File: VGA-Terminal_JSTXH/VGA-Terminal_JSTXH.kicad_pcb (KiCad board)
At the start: 2 copper layers, 51 x 44 mm, 12 parts, among them J1 DB15_Female_HighDensity_Mount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, J2 Thermistor, J3 Heater, J4 E3D Fan, J5 X Endstop, J6 Z Endstop, J7 GND & Pin14, J8 Part Fan, J9 Always On Fan

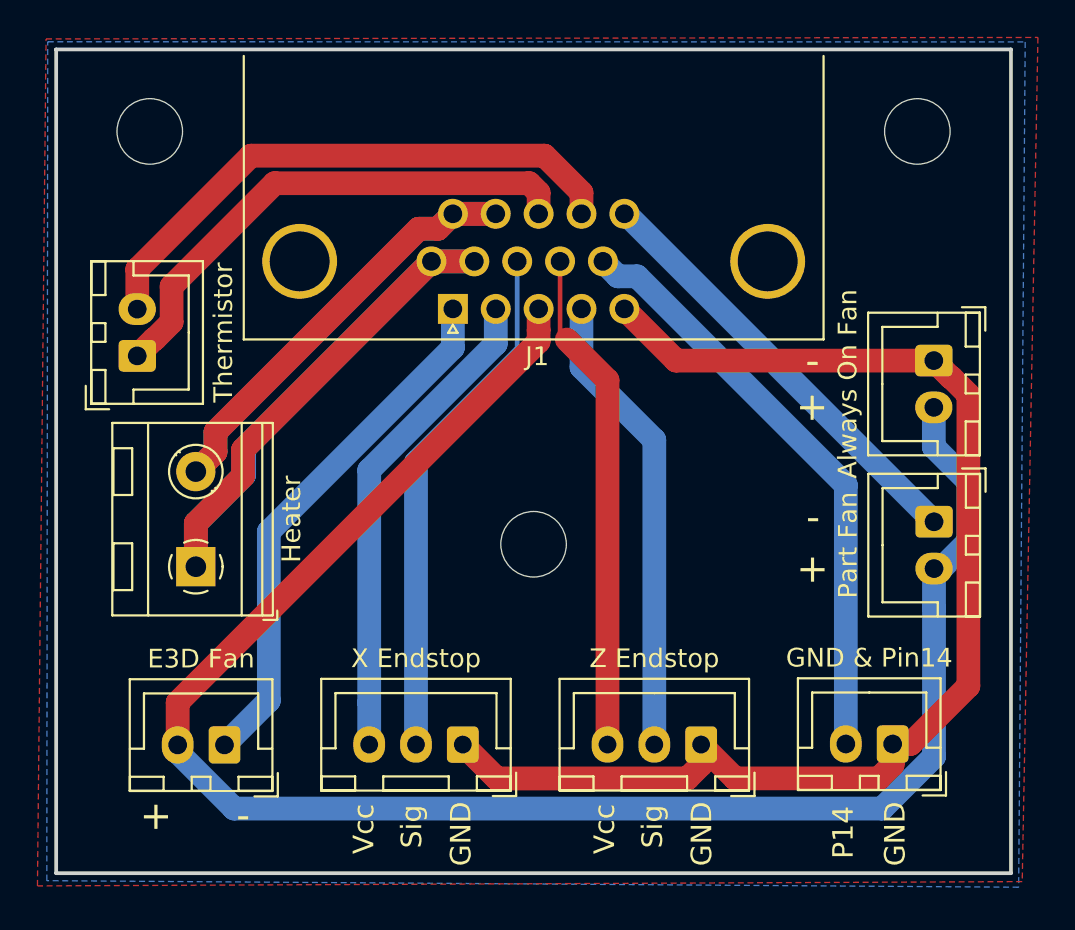
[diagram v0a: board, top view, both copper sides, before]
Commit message: - Replaced the footprints - Added a additional screw terminal for the custom pin 14
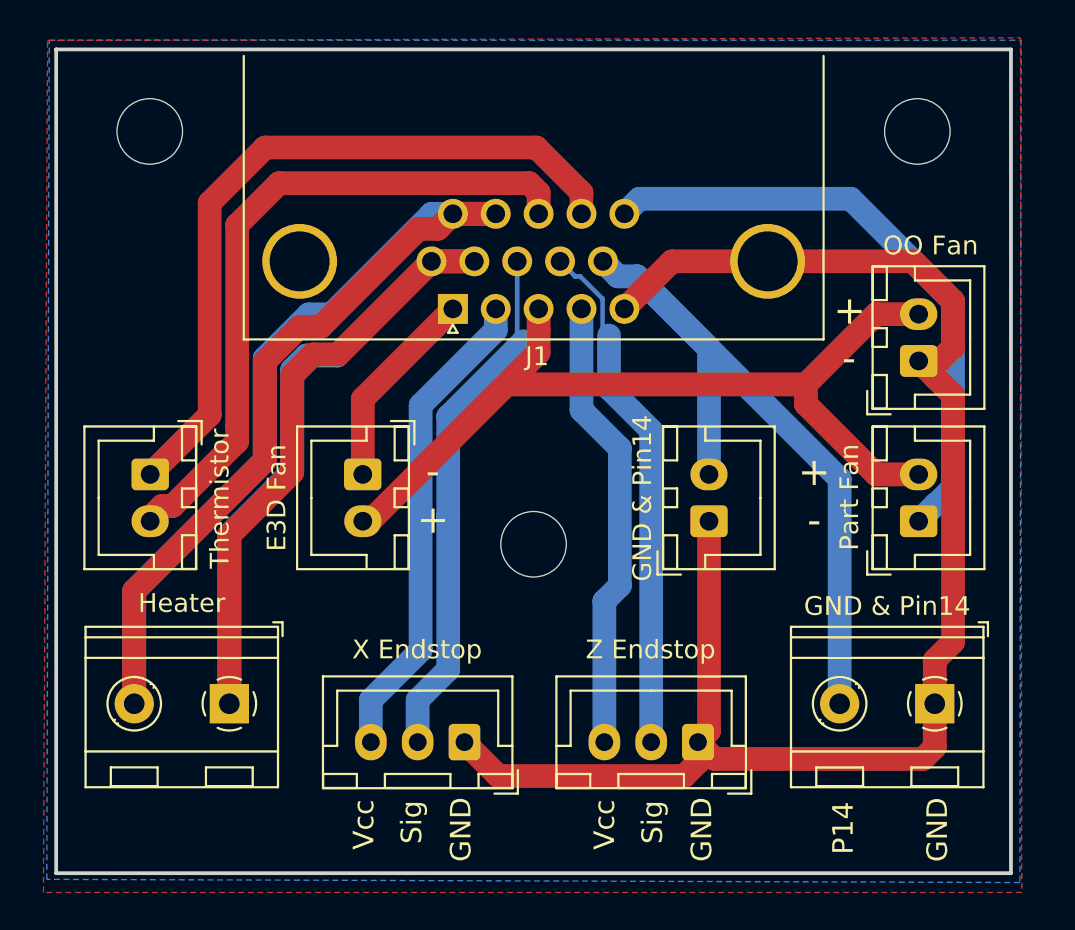
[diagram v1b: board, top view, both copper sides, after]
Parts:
- added J10: GND & Pin14, TerminalBlock_RND:TerminalBlock_RND_205-00232_1x02_P5.08mm_Horizontal, F.Cu at (134.9, 97.0)
- J9: value Always On Fan -> OO Fan
- moved J4 16.2 mm to (104.4, 84.7), turned to 270 degrees
- moved J7 15.4 mm to (122.9, 87.2), turned to 90 degrees
- moved J3 7.54 mm to (97.2, 97.0), turned to 180 degrees
- moved J2 6.37 mm to (93.0, 84.7), turned to 270 degrees
- moved J8 0.82 mm to (134.1, 87.2), turned to 90 degrees
- moved J9 0.81 mm to (134.1, 78.6), turned to 90 degrees
- moved J6 0.21 mm to (122.3, 99.0)
- moved J5 0.16 mm to (109.8, 99.0)
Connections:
- J1 pad 4: Z_Sig -> Vcc_Z
- J1 pad 9: Vcc_Z -> Z_Sig
- J2 pad 1: THERM_B -> THERM_A
- J2 pad 2: THERM_A -> THERM_B
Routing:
- net V_FAN: track 94.9 -> 47.6 mm
- net HOT_A: track 44.7 -> 73.6 mm
- net E3D_N: track 28.3 -> 10.8 mm
- net GND: track 68.4 -> 85.8 mm
- net HOT_B: track 47.6 -> 62.5 mm
- net Pin14: track 31.8 -> 41.6 mm
- net Part_N: track 23.4 -> 32.7 mm
- net THERM_B: track 27.7 -> 36.4 mm
- net THERM_A: track 30.3 -> 39.0 mm
- net Z_Sig: track 24.9 -> 27.9 mm
- net Vcc_Z: track 26.9 -> 24.3 mm
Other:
- board text added: "v0.3 / 2019-02-14"
- board text removed: "v0.3 / 2019-02-13"
